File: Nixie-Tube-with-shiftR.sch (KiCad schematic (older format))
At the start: 51 parts, among them J1 Conn_01x05_Male, J2 Conn_01x01_Female, J3 Conn_01x05_Female, J4 Conn_01x01_Male, Q1 MMBTA42LT1, Q10 MMBTA42LT1, Q11 AO3400, Q12 AO3400, Q13 AO3400, Q14 MMBTA42LT1, Q2 MMBTA42LT1, Q3 MMBTA42LT1, Q4 MMBTA42LT1, Q5 MMBTA42LT1, Q6 MMBTA42LT1, Q7 MMBTA42LT1, Q8 MMBTA42LT1, Q9 MMBTA42LT1, U1 74HC595D, U2 nixie-tube, U3 74HC595D, U4 MIC5219-5.0

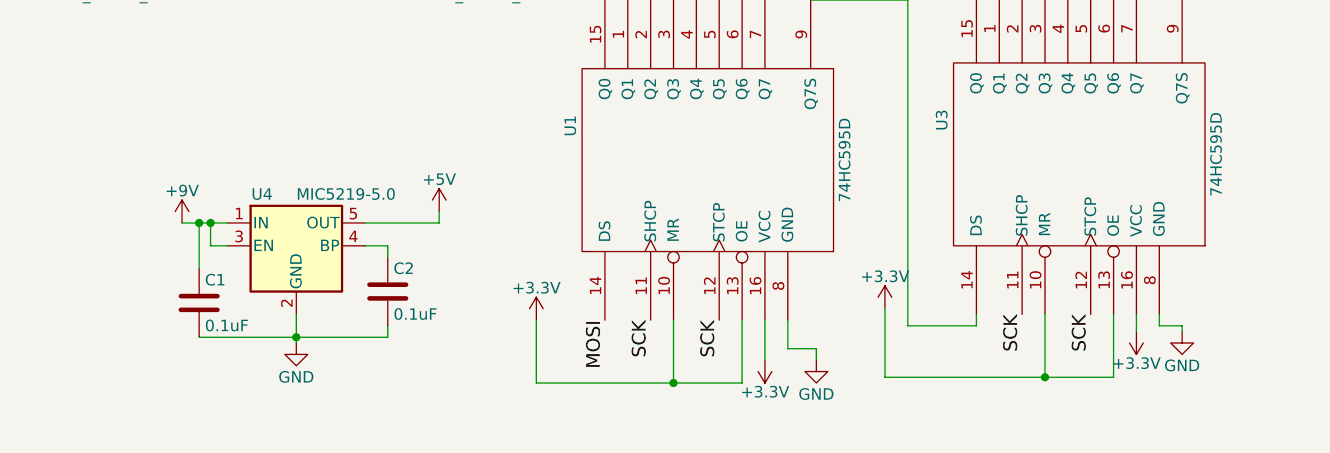
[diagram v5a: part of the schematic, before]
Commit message: route all components but ground
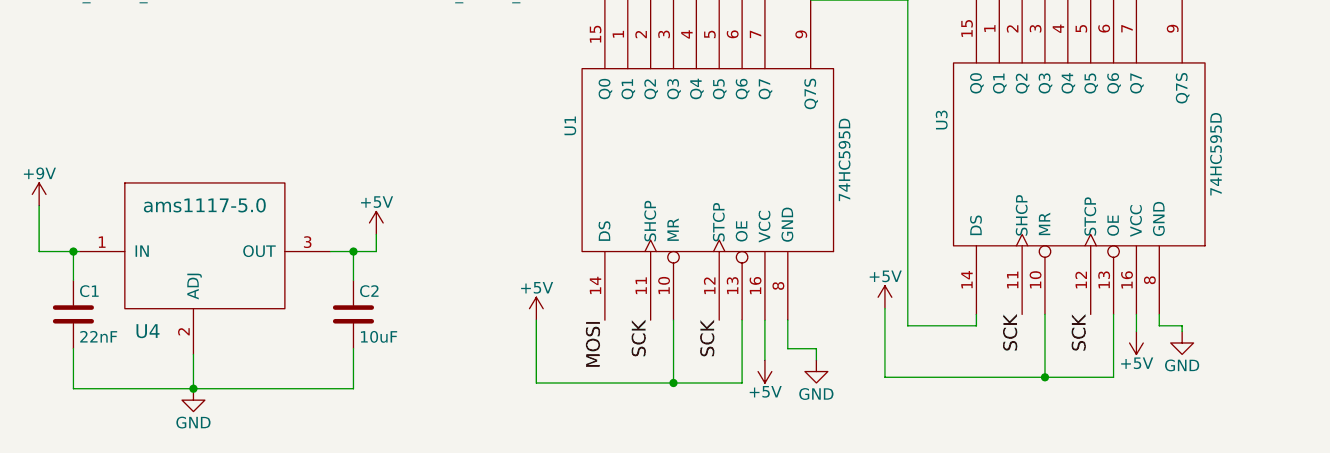
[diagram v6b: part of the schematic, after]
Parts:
- removed U4: MIC5219-5.0, TO_SOT_Packages_SMD:SOT-23-5, symbol MIC5219-5.0
- added U4: ams1117-5.0, TO_SOT_Packages_SMD:SOT-223-3Lead_TabPin2, symbol ams1117-5.0
- C1: value 0.1uF -> 22nF; footprint (none) -> Capacitors_SMD:C_0603
- C2: value 0.1uF -> 10uF; footprint (none) -> Capacitors_SMD:C_0603
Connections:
- net labels removed: +3.3V
- wire segments 62 -> 61
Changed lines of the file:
@@
 	7325 3125 7325 3200
 $Comp
-L GND #PWR13
+L GND #PWR01
 U 1 1 59DF0537
 P 7325 3200
-F 0 "#PWR13" H 7325 2950 50  0001 C CNN
+F 0 "#PWR01" H 7325 2950 50  0001 C CNN
 F 1 "GND" H 7325 3050 50  0000 C CNN
 F 2 "" H 7325 3200 50  0001 C CNN
@@
 	6950 3775 6950 3850
 $Comp
-L GND #PWR12
+L GND #PWR02
 U 1 1 59DF0997
 P 6950 3850
-F 0 "#PWR12" H 6950 3600 50  0001 C CNN
+F 0 "#PWR02" H 6950 3600 50  0001 C CNN
 F 1 "GND" H 6950 3700 50  0000 C CNN
 F 2 "" H 6950 3850 50  0001 C CNN
@@
 	4925 5800 4925 5850
 $Comp
-L GND #PWR8
+L GND #PWR03
 U 1 1 59DEF495
 P 4925 5850
-F 0 "#PWR8" H 4925 5600 50  0001 C CNN
+F 0 "#PWR03" H 4925 5600 50  0001 C CNN
 F 1 "GND" H 4925 5700 50  0000 C CNN
 F 2 "" H 4925 5850 50  0001 C CNN
@@
 	6325 5650 6325 5725
 $Comp
-L GND #PWR11
+L GND #PWR04
 U 1 1 59DEFAF9
 P 6525 5725
-F 0 "#PWR11" H 6525 5475 50  0001 C CNN
+F 0 "#PWR04" H 6525 5475 50  0001 C CNN
 F 1 "GND" H 6525 5575 50  0000 C CNN
 F 2 "" H 6525 5725 50  0001 C CNN
@@
 $EndComp
 $Comp
-L GND #PWR17
+L GND #PWR05
 U 1 1 59DF166A
 P 8375 5950
-F 0 "#PWR17" H 8375 5700 50  0001 C CNN
+F 0 "#PWR05" H 8375 5700 50  0001 C CNN
 F 1 "GND" H 8375 5800 50  0000 C CNN
 F 2 "" H 8375 5950 50  0001 C CNN
@@
 Dot
 $Comp
-L GND #PWR16
+L GND #PWR06
 U 1 1 59E03A8E
 P 8350 3825
-F 0 "#PWR16" H 8350 3575 50  0001 C CNN
+F 0 "#PWR06" H 8350 3575 50  0001 C CNN
 F 1 "GND" H 8350 3675 50  0000 C CNN
 F 2 "" H 8350 3825 50  0001 C CNN
@@
 Connection ~ 5925 5925
 $Comp
-L +9V #PWR2
+L +9V #PWR07
 U 1 1 59E07785
 P 2575 3175
-F 0 "#PWR2" H 2575 3025 50  0001 C CNN
+F 0 "#PWR07" H 2575 3025 50  0001 C CNN
 F 1 "+9V" H 2575 3315 50  0000 C CNN
 F 2 "" H 2575 3175 50  0001 C CNN
@@
 Connection ~ 2575 4150
 $Comp
-L GND #PWR4
+L GND #PWR08
 U 1 1 59E07C89
 P 2800 3525
-F 0 "#PWR4" H 2800 3275 50  0001 C CNN
+F 0 "#PWR08" H 2800 3275 50  0001 C CNN
 F 1 "GND" H 2800 3375 50  0000 C CNN
 F 2 "" H 2800 3525 50  0001 C CNN
@@
 Connection ~ 2800 3950
 $Comp
-L +9V #PWR14
+L +9V #PWR09
 U 1 1 59E08805
 P 8025 4650
-F 0 "#PWR14" H 8025 4500 50  0001 C CNN
+F 0 "#PWR09" H 8025 4500 50  0001 C CNN
 F 1 "+9V" H 8025 4790 50  0000 C CNN
 F 2 "" H 8025 4650 50  0001 C CNN
@@
 $EndComp
 $Comp
-L +9V #PWR18
+L +9V #PWR010
 U 1 1 59E088D3
 P 8925 4675
-F 0 "#PWR18" H 8925 4525 50  0001 C CNN
+F 0 "#PWR010" H 8925 4525 50  0001 C CNN
 F 1 "+9V" H 8925 4815 50  0000 C CNN
 F 2 "" H 8925 4675 50  0001 C CNN
@@
 $EndComp
 $Comp
-L +9V #PWR19
+L +9V #PWR011
 U 1 1 59E0896B
 P 9700 4675
-F 0 "#PWR19" H 9700 4525 50  0001 C CNN
+F 0 "#PWR011" H 9700 4525 50  0001 C CNN
 F 1 "+9V" H 9700 4815 50  0000 C CNN
 F 2 "" H 9700 4675 50  0001 C CNN
@@
 $EndComp
 $Comp
-L +9V #PWR1
-U 1 1 59E0C504
-P 2150 5250
-F 0 "#PWR1" H 2150 5100 50  0001 C CNN
-F 1 "+9V" H 2150 5390 50  0000 C CNN
-F 2 "" H 2150 5250 50  0001 C CNN
-F 3 "" H 2150 5250 50  0001 C CNN
-	1    2150 5250
-	1    0    0    -1
-$EndComp
-Wire Wire Line
-	2150 5250 2350 5250
-Wire Wire Line
-	2950 5250 3275 5250
-Wire Wire Line
-	3275 5250 3275 5200
-Wire Wire Line
-	2350 5350 2275 5350
-Wire Wire Line
-	2275 5350 2275 5250
-Connection ~ 2275 5250
-$Comp
-L GND #PWR3
-U 1 1 59E0D231
-P 2650 5775
-F 0 "#PWR3" H 2650 5525 50  0001 C CNN
-F 1 "GND" H 2650 5625 50  0000 C CNN
-F 2 "" H 2650 5775 50  0001 C CNN
-F 3 "" H 2650 5775 50  0001 C CNN
-	1    2650 5775
-	1    0    0    -1
-$EndComp
-$Comp
-L +3.3V #PWR6
-U 1 1 59E0E086
-P 3700 5675
-F 0 "#PWR6" H 3700 5525 50  0001 C CNN
-F 1 "+3.3V" H 3700 5815 50  0000 C CNN
-F 2 "" H 3700 5675 50  0001 C CNN
-F 3 "" H 3700 5675 50  0001 C CNN
-	1    3700 5675
-	1    0    0    -1
-$EndComp
-$Comp
-L +3.3V #PWR9
-U 1 1 59E0E12B
-P 5225 5625
-F 0 "#PWR9" H 5225 5475 50  0001 C CNN
-F 1 "+3.3V" H 5225 5765 50  0000 C CNN
-F 2 "" H 5225 5625 50  0001 C CNN
-F 3 "" H 5225 5625 50  0001 C CNN
-	1    5225 5625
-	1    0    0    -1
-$EndComp
-$Comp
-L +3.3V #PWR7
-U 1 1 59E0E267
-P 4700 5850
-F 0 "#PWR7" H 4700 5700 50  0001 C CNN
-F 1 "+3.3V" H 4700 5990 50  0000 C CNN
-F 2 "" H 4700 5850 50  0001 C CNN
-F 3 "" H 4700 5850 50  0001 C CNN
-	1    4700 5850
-	-1   0    0    1
-$EndComp
-$Comp
-L +3.3V #PWR10
-U 1 1 59E0E3FE
-P 6325 5725
-F 0 "#PWR10" H 6325 5575 50  0001 C CNN
-F 1 "+3.3V" H 6325 5865 50  0000 C CNN
-F 2 "" H 6325 5725 50  0001 C CNN
-F 3 "" H 6325 5725 50  0001 C CNN
-	1    6325 5725
-	-1   0    0    1
-$EndComp
-$Comp
-L C C1
-U 1 1 59E1233C
-P 2225 5600
-F 0 "C1" H 2250 5700 50  0000 L CNN
-F 1 "0.1uF" H 2250 5500 50  0000 L CNN
-F 2 "" H 2263 5450 50  0001 C CNN
-F 3 "" H 2225 5600 50  0001 C CNN
-	1    2225 5600
-	1    0    0    -1
-$EndComp
-Wire Wire Line
-	2225 5250 2225 5450
-Connection ~ 2225 5250
-Wire Wire Line
-	2225 5750 3050 5750
-Wire Wire Line
-	2650 5650 2650 5775
-Connection ~ 2650 5750
-$Comp
-L C C2
-U 1 1 59E1285B
-P 3050 5550
-F 0 "C2" H 3075 5650 50  0000 L CNN
-F 1 "0.1uF" H 3075 5450 50  0000 L CNN
-F 2 "" H 3088 5400 50  0001 C CNN
-F 3 "" H 3050 5550 50  0001 C CNN
-	1    3050 5550
-	1    0    0    -1
-$EndComp
-Wire Wire Line
-	2950 5350 3050 5350
-Wire Wire Line
-	3050 5350 3050 5400
-Wire Wire Line
-	3050 5750 3050 5700
-$Comp
-L +9V #PWR15
+L +9V #PWR012
 U 1 1 59E167E2
 P 8350 2825
-F 0 "#PWR15" H 8350 2675 50  0001 C CNN
+F 0 "#PWR012" H 8350 2675 50  0001 C CNN
 F 1 "+9V" H 8350 2965 50  0000 C CNN
 F 2 "" H 8350 2825 50  0001 C CNN
@@
 Connection ~ 4475 1700
 $Comp
-L MIC5219-5.0 U4
-U 1 1 59DFA48B
-P 2650 5350
-F 0 "U4" H 2500 5575 50  0000 C CNN
-F 1 "MIC5219-5.0" H 2650 5575 50  0000 L CNN
-F 2 "TO_SOT_Packages_SMD:SOT-23-5" H 2650 5675 50  0001 C CNN
-F 3 "" H 2650 5350 50  0001 C CNN
-	1    2650 5350
-	1    0    0    -1
-$EndComp
-$Comp
-L +5V #PWR5
-U 1 1 59DFA725
-P 3275 5200
-F 0 "#PWR5" H 3275 5050 50  0001 C CNN
-F 1 "+5V" H 3275 5340 50  0000 C CNN
-F 2 "" H 3275 5200 50  0000 C CNN
-F 3 "" H 3275 5200 50  0000 C CNN
-	1    3275 5200
-	1    0    0    -1
+L ams1117-5.0 U4
+U 1 1 59E0C66F
+P 1950 5275
+F 0 "U4" H 2000 4825 60  0000 C CNN
+F 1 "ams1117-5.0" H 2250 5375 60  0000 C CNN
+F 2 "TO_SOT_Packages_SMD:SOT-223-3Lead_TabPin2" H 1950 5275 60  0001 C CNN
+F 3 "" H 1950 5275 60  0001 C CNN
+	1    1950 5275
+	1    0    0    -1
+$EndComp
+$Comp
+L +9V #PWR013
+U 1 1 59E0CD5E
+P 1525 5175
+F 0 "#PWR013" H 1525 5025 50  0001 C CNN
+F 1 "+9V" H 1525 5315 50  0000 C CNN
+F 2 "" H 1525 5175 50  0001 C CNN
+F 3 "" H 1525 5175 50  0001 C CNN
+	1    1525 5175
+	1    0    0    -1
+$EndComp
+Wire Wire Line
+	1525 5175 1525 5375
+Wire Wire Line
+	1525 5375 1700 5375
+$Comp
+L +5V #PWR014
+U 1 1 59E0CEE2
+P 3000 5300
+F 0 "#PWR014" H 3000 5150 50  0001 C CNN
+F 1 "+5V" H 3000 5440 50  0000 C CNN
+F 2 "" H 3000 5300 50  0001 C CNN
+F 3 "" H 3000 5300 50  0001 C CNN
+	1    3000 5300
+	1    0    0    -1
+$EndComp
+Wire Wire Line
+	2800 5375 3000 5375
+Wire Wire Line
+	3000 5375 3000 5300
+$Comp
+L GND #PWR015
+U 1 1 59E0CFCB
+P 2200 5975
+F 0 "#PWR015" H 2200 5725 50  0001 C CNN
+F 1 "GND" H 2200 5825 50  0000 C CNN
+F 2 "" H 2200 5975 50  0001 C CNN
+F 3 "" H 2200 5975 50  0001 C CNN
+	1    2200 5975
+	1    0    0    -1
+$EndComp
+$Comp
+L C C1
+U 1 1 59E0D041
+P 1675 5650
+F 0 "C1" H 1700 5750 50  0000 L CNN
+F 1 "22nF" H 1700 5550 50  0000 L CNN
+F 2 "Capacitors_SMD:C_0603" H 1713 5500 50  0001 C CNN
+F 3 "" H 1675 5650 50  0001 C CNN
+	1    1675 5650
+	1    0    0    -1
+$EndComp
+$Comp
+L C C2
+U 1 1 59E0D25C
+P 2900 5650
+F 0 "C2" H 2925 5750 50  0000 L CNN
+F 1 "10uF" H 2925 5550 50  0000 L CNN
+F 2 "Capacitors_SMD:C_0603" H 2938 5500 50  0001 C CNN
+F 3 "" H 2900 5650 50  0001 C CNN
+	1    2900 5650
+	1    0    0    -1
+$EndComp
+Wire Wire Line
+	1675 5500 1675 5375
+Connection ~ 1675 5375
+Wire Wire Line
+	2900 5500 2900 5375
+Connection ~ 2900 5375
+Wire Wire Line
+	1675 5800 1675 5975
+Wire Wire Line
+	1675 5975 2900 5975
+Wire Wire Line
+	2900 5975 2900 5800
+Connection ~ 2200 5975
+Wire Wire Line
+	2200 5825 2200 5975
+$Comp
+L +5V #PWR016
+U 1 1 59E0E450
+P 3700 5675
+F 0 "#PWR016" H 3700 5525 50  0001 C CNN
+F 1 "+5V" H 3700 5815 50  0000 C CNN
+F 2 "" H 3700 5675 50  0001 C CNN
+F 3 "" H 3700 5675 50  0001 C CNN
+	1    3700 5675
+	1    0    0    -1
+$EndComp
+$Comp
+L +5V #PWR017
+U 1 1 59E0E605
+P 4700 5850
+F 0 "#PWR017" H 4700 5700 50  0001 C CNN
+F 1 "+5V" H 4700 5990 50  0000 C CNN
+F 2 "" H 4700 5850 50  0001 C CNN
+F 3 "" H 4700 5850 50  0001 C CNN
+	1    4700 5850
+	-1   0    0    1
+$EndComp
+$Comp
+L +5V #PWR018
+U 1 1 59E0EA7E
+P 5225 5625
+F 0 "#PWR018" H 5225 5475 50  0001 C CNN
+F 1 "+5V" H 5225 5765 50  0000 C CNN
+F 2 "" H 5225 5625 50  0001 C CNN
+F 3 "" H 5225 5625 50  0001 C CNN
+	1    5225 5625
+	1    0    0    -1
+$EndComp
+$Comp
+L +5V #PWR019
+U 1 1 59E0EB56
+P 6325 5725
+F 0 "#PWR019" H 6325 5575 50  0001 C CNN
+F 1 "+5V" H 6325 5865 50  0000 C CNN
+F 2 "" H 6325 5725 50  0001 C CNN
+F 3 "" H 6325 5725 50  0001 C CNN
+	1    6325 5725
+	-1   0    0    1
 $EndComp
 $EndSCHEMATC

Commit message: placed all the component
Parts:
- removed D2: Dot_LED, symbol LED-RESCUE-Nixie-Tube-with-shiftR
- removed U2: nixie-tube, nixie-tube-fp:qs30-1, symbol nixie-tube
- added NE1: Lamp_Neon_Up, nixie-tube-fp:neon-tube, symbol Lamp_Neon
- added NE2: Lamp_Neon_Down, nixie-tube-fp:neon-tube, symbol Lamp_Neon
- added Q15: MMBTA42LT1, TO_SOT_Packages_SMD:SOT-23, symbol Q_NPN_BCE
- added R26, R27: R, Resistors_SMD:R_0603, symbol R
- added U2: nixie-tube-qs27, nixie-tube-fp:qs27-1, symbol nixie-tube-qs27
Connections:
- net labels added: DotD, DotU
- net labels removed: Dot
- wire segments 61 -> 63
- no-connect marks 4 -> 1
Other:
- moved on the sheet: Q14, R24, R25
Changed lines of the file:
@@
 Comment4 ""
 $EndDescr
-$Comp
-L nixie-tube U2
-U 1 1 59DE1F0A
-P 5450 1950
-F 0 "U2" H 4850 2550 60  0000 C CNN
-F 1 "nixie-tube" H 5450 2350 60  0000 C CNN
-F 2 "nixie-tube-fp:qs30-1" H 5150 1950 60  0001 C CNN
-F 3 "" H 5150 1950 60  0001 C CNN
-	1    5450 1950
-	1    0    0    -1
-$EndComp
 Text Notes 4000 1700 0    60   ~ 0
 180V
@@
 Wire Wire Line
 	6525 5700 6525 5725
-NoConn ~ 6225 4250
 NoConn ~ 6325 4250
 $Comp
@@
 	1    0    0    -1
 $EndComp
-NoConn ~ 5025 1325
-NoConn ~ 5150 1325
 $Comp
 L Conn_01x01_Female J2
@@
 MOSI-OUT
 $Comp
-L LED-RESCUE-Nixie-Tube-with-shiftR D2
-U 1 1 59E02618
-P 8350 2975
-F 0 "D2" H 8350 3075 50  0000 C CNN
-F 1 "Dot_LED" H 8350 2875 50  0000 C CNN
-F 2 "" H 8350 2975 50  0001 C CNN
-F 3 "" H 8350 2975 50  0001 C CNN
-	1    8350 2975
-	0    -1   -1   0
-$EndComp
-$Comp
 L Q_NPN_BCE Q14
 U 1 1 59E02747
-P 8250 3625
-F 0 "Q14" H 8450 3675 50  0000 L CNN
-F 1 "MMBTA42LT1" H 8450 3575 50  0000 L CNN
-F 2 "TO_SOT_Packages_SMD:SOT-23" H 8450 3725 50  0001 C CNN
-F 3 "" H 8250 3625 50  0001 C CNN
-	1    8250 3625
+P 7675 2150
+F 0 "Q14" H 7875 2200 50  0000 L CNN
+F 1 "MMBTA42LT1" H 7875 2100 50  0000 L CNN
+F 2 "TO_SOT_Packages_SMD:SOT-23" H 7875 2250 50  0001 C CNN
+F 3 "" H 7675 2150 50  0001 C CNN
+	1    7675 2150
 	1    0    0    -1
 $EndComp
@@
 L R R24
 U 1 1 59E037C1
-P 8050 3475
-F 0 "R24" V 8130 3475 50  0000 C CNN
-F 1 "R" V 8050 3475 50  0000 C CNN
-F 2 "Resistors_SMD:R_0603" V 7980 3475 50  0001 C CNN
-F 3 "" H 8050 3475 50  0001 C CNN
-	1    8050 3475
+P 7475 2000
+F 0 "R24" V 7555 2000 50  0000 C CNN
+F 1 "R" V 7475 2000 50  0000 C CNN
+F 2 "Resistors_SMD:R_0603" V 7405 2000 50  0001 C CNN
+F 3 "" H 7475 2000 50  0001 C CNN
+	1    7475 2000
 	1    0    0    -1
 $EndComp
 Text Label 6125 4250 1    60   ~ 0
-Dot
-Text Label 8050 3325 2    60   ~ 0
-Dot
+DotU
+Text Label 7475 1850 2    60   ~ 0
+DotU
 $Comp
 L GND #PWR06
 U 1 1 59E03A8E
-P 8350 3825
-F 0 "#PWR06" H 8350 3575 50  0001 C CNN
-F 1 "GND" H 8350 3675 50  0000 C CNN
-F 2 "" H 8350 3825 50  0001 C CNN
-F 3 "" H 8350 3825 50  0001 C CNN
-	1    8350 3825
+P 7775 2350
+F 0 "#PWR06" H 7775 2100 50  0001 C CNN
+F 1 "GND" H 7775 2200 50  0000 C CNN
+F 2 "" H 7775 2350 50  0001 C CNN
+F 3 "" H 7775 2350 50  0001 C CNN
+	1    7775 2350
 	1    0    0    -1
 $EndComp
@@
 L R R25
 U 1 1 59E03B9C
-P 8350 3275
-F 0 "R25" V 8430 3275 50  0000 C CNN
-F 1 "R" V 8350 3275 50  0000 C CNN
-F 2 "Resistors_SMD:R_0603" V 8280 3275 50  0001 C CNN
-F 3 "" H 8350 3275 50  0001 C CNN
-	1    8350 3275
+P 7775 1800
+F 0 "R25" V 7855 1800 50  0000 C CNN
+F 1 "R" V 7775 1800 50  0000 C CNN
+F 2 "Resistors_SMD:R_0603" V 7705 1800 50  0001 C CNN
+F 3 "" H 7775 1800 50  0001 C CNN
+	1    7775 1800
 	1    0    0    -1
 $EndComp
@@
 	1    0    0    -1
 $EndComp
-$Comp
-L +9V #PWR012
-U 1 1 59E167E2
-P 8350 2825
-F 0 "#PWR012" H 8350 2675 50  0001 C CNN
-F 1 "+9V" H 8350 2965 50  0000 C CNN
-F 2 "" H 8350 2825 50  0001 C CNN
-F 3 "" H 8350 2825 50  0001 C CNN
-	1    8350 2825
-	1    0    0    -1
-$EndComp
 Text Label 5000 2375 0    60   ~ 0
 n0
@@
 	4475 1700 4475 1175
 Wire Wire Line
-	4475 1175 6525 1175
+	4475 1175 8725 1175
 Wire Wire Line
 	6525 1175 6525 1700
@@
 $EndComp
 $Comp
-L +9V #PWR013
+L +9V #PWR012
 U 1 1 59E0CD5E
 P 1525 5175
-F 0 "#PWR013" H 1525 5025 50  0001 C CNN
+F 0 "#PWR012" H 1525 5025 50  0001 C CNN
 F 1 "+9V" H 1525 5315 50  0000 C CNN
 F 2 "" H 1525 5175 50  0001 C CNN
@@
 	1525 5375 1700 5375
 $Comp
-L +5V #PWR014
+L +5V #PWR013
 U 1 1 59E0CEE2
 P 3000 5300
-F 0 "#PWR014" H 3000 5150 50  0001 C CNN
+F 0 "#PWR013" H 3000 5150 50  0001 C CNN
 F 1 "+5V" H 3000 5440 50  0000 C CNN
 F 2 "" H 3000 5300 50  0001 C CNN
@@
 	3000 5375 3000 5300
 $Comp
-L GND #PWR015
+L GND #PWR014
 U 1 1 59E0CFCB
 P 2200 5975
-F 0 "#PWR015" H 2200 5725 50  0001 C CNN
+F 0 "#PWR014" H 2200 5725 50  0001 C CNN
 F 1 "GND" H 2200 5825 50  0000 C CNN
 F 2 "" H 2200 5975 50  0001 C CNN
@@
 	2200 5825 2200 5975
 $Comp
-L +5V #PWR016
+L +5V #PWR015
 U 1 1 59E0E450
 P 3700 5675
-F 0 "#PWR016" H 3700 5525 50  0001 C CNN
+F 0 "#PWR015" H 3700 5525 50  0001 C CNN
 F 1 "+5V" H 3700 5815 50  0000 C CNN
 F 2 "" H 3700 5675 50  0001 C CNN
@@
 $EndComp
 $Comp
-L +5V #PWR017
+L +5V #PWR016
 U 1 1 59E0E605
 P 4700 5850
-F 0 "#PWR017" H 4700 5700 50  0001 C CNN
+F 0 "#PWR016" H 4700 5700 50  0001 C CNN
 F 1 "+5V" H 4700 5990 50  0000 C CNN
 F 2 "" H 4700 5850 50  0001 C CNN
@@
 $EndComp
 $Comp
-L +5V #PWR018
+L +5V #PWR017
 U 1 1 59E0EA7E
 P 5225 5625
-F 0 "#PWR018" H 5225 5475 50  0001 C CNN
+F 0 "#PWR017" H 5225 5475 50  0001 C CNN
 F 1 "+5V" H 5225 5765 50  0000 C CNN
 F 2 "" H 5225 5625 50  0001 C CNN
@@
 $EndComp
 $Comp
-L +5V #PWR019
+L +5V #PWR018
 U 1 1 59E0EB56
 P 6325 5725
-F 0 "#PWR019" H 6325 5575 50  0001 C CNN
+F 0 "#PWR018" H 6325 5575 50  0001 C CNN
 F 1 "+5V" H 6325 5865 50  0000 C CNN
 F 2 "" H 6325 5725 50  0001 C CNN
@@
 	-1   0    0    1
 $EndComp
+$Comp
+L nixie-tube-qs27 U2
+U 1 1 59E1ACBC
+P 5450 1950
+F 0 "U2" H 4875 2050 60  0000 C CNN
+F 1 "nixie-tube-qs27" H 5625 2275 60  0000 C CNN
+F 2 "nixie-tube-fp:qs27-1" H 5150 1975 60  0001 C CNN
+F 3 "" H 5150 1975 60  0001 C CNN
+	1    5450 1950
+	1    0    0    -1
+$EndComp
+Wire Wire Line
+	7775 1175 7775 1250
+Connection ~ 6525 1175
+$Comp
+L Q_NPN_BCE Q15
+U 1 1 59E1EE85
+P 8625 2150
+F 0 "Q15" H 8825 2200 50  0000 L CNN
+F 1 "MMBTA42LT1" H 8825 2100 50  0000 L CNN
+F 2 "TO_SOT_Packages_SMD:SOT-23" H 8825 2250 50  0001 C CNN
+F 3 "" H 8625 2150 50  0001 C CNN
+	1    8625 2150
+	1    0    0    -1
+$EndComp
+$Comp
+L R R26
+U 1 1 59E1EE8B
+P 8425 2000
+F 0 "R26" V 8505 2000 50  0000 C CNN
+F 1 "R" V 8425 2000 50  0000 C CNN
+F 2 "Resistors_SMD:R_0603" V 8355 2000 50  0001 C CNN
+F 3 "" H 8425 2000 50  0001 C CNN
+	1    8425 2000
+	1    0    0    -1
+$EndComp
+Text Label 8425 1850 2    60   ~ 0
+DotD
+$Comp
+L GND #PWR019
+U 1 1 59E1EE92
+P 8725 2350
+F 0 "#PWR019" H 8725 2100 50  0001 C CNN
+F 1 "GND" H 8725 2200 50  0000 C CNN
+F 2 "" H 8725 2350 50  0001 C CNN
+F 3 "" H 8725 2350 50  0001 C CNN
+	1    8725 2350
+	1    0    0    -1
+$EndComp
+$Comp
+L R R27
+U 1 1 59E1EE98
+P 8725 1800
+F 0 "R27" V 8805 1800 50  0000 C CNN
+F 1 "R" V 8725 1800 50  0000 C CNN
+F 2 "Resistors_SMD:R_0603" V 8655 1800 50  0001 C CNN
+F 3 "" H 8725 1800 50  0001 C CNN
+	1    8725 1800
+	1    0    0    -1
+$EndComp
+Wire Wire Line
+	8725 1175 8725 1250
+Connection ~ 7775 1175
+$Comp
+L Lamp_Neon NE1
+U 1 1 59E2014E
+P 7775 1450
+F 0 "NE1" H 7800 1600 50  0000 L CNN
+F 1 "Lamp_Neon_Up" H 7800 1300 50  0000 L CNN
+F 2 "nixie-tube-fp:neon-tube" V 7775 1550 50  0001 C CNN
+F 3 "" V 7775 1550 50  0001 C CNN
+	1    7775 1450
+	-1   0    0    1
+$EndComp
+$Comp
+L Lamp_Neon NE2
+U 1 1 59E20B86
+P 8725 1450
+F 0 "NE2" H 8750 1600 50  0000 L CNN
+F 1 "Lamp_Neon_Down" H 8750 1300 50  0000 L CNN
+F 2 "nixie-tube-fp:neon-tube" V 8725 1550 50  0001 C CNN
+F 3 "" V 8725 1550 50  0001 C CNN
+	1    8725 1450
+	-1   0    0    1
+$EndComp
+Text Label 6225 4250 1    60   ~ 0
+DotD
 $EndSCHEMATC
